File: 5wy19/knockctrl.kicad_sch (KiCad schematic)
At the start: 1 part, among them IC5 TP1C8101DW

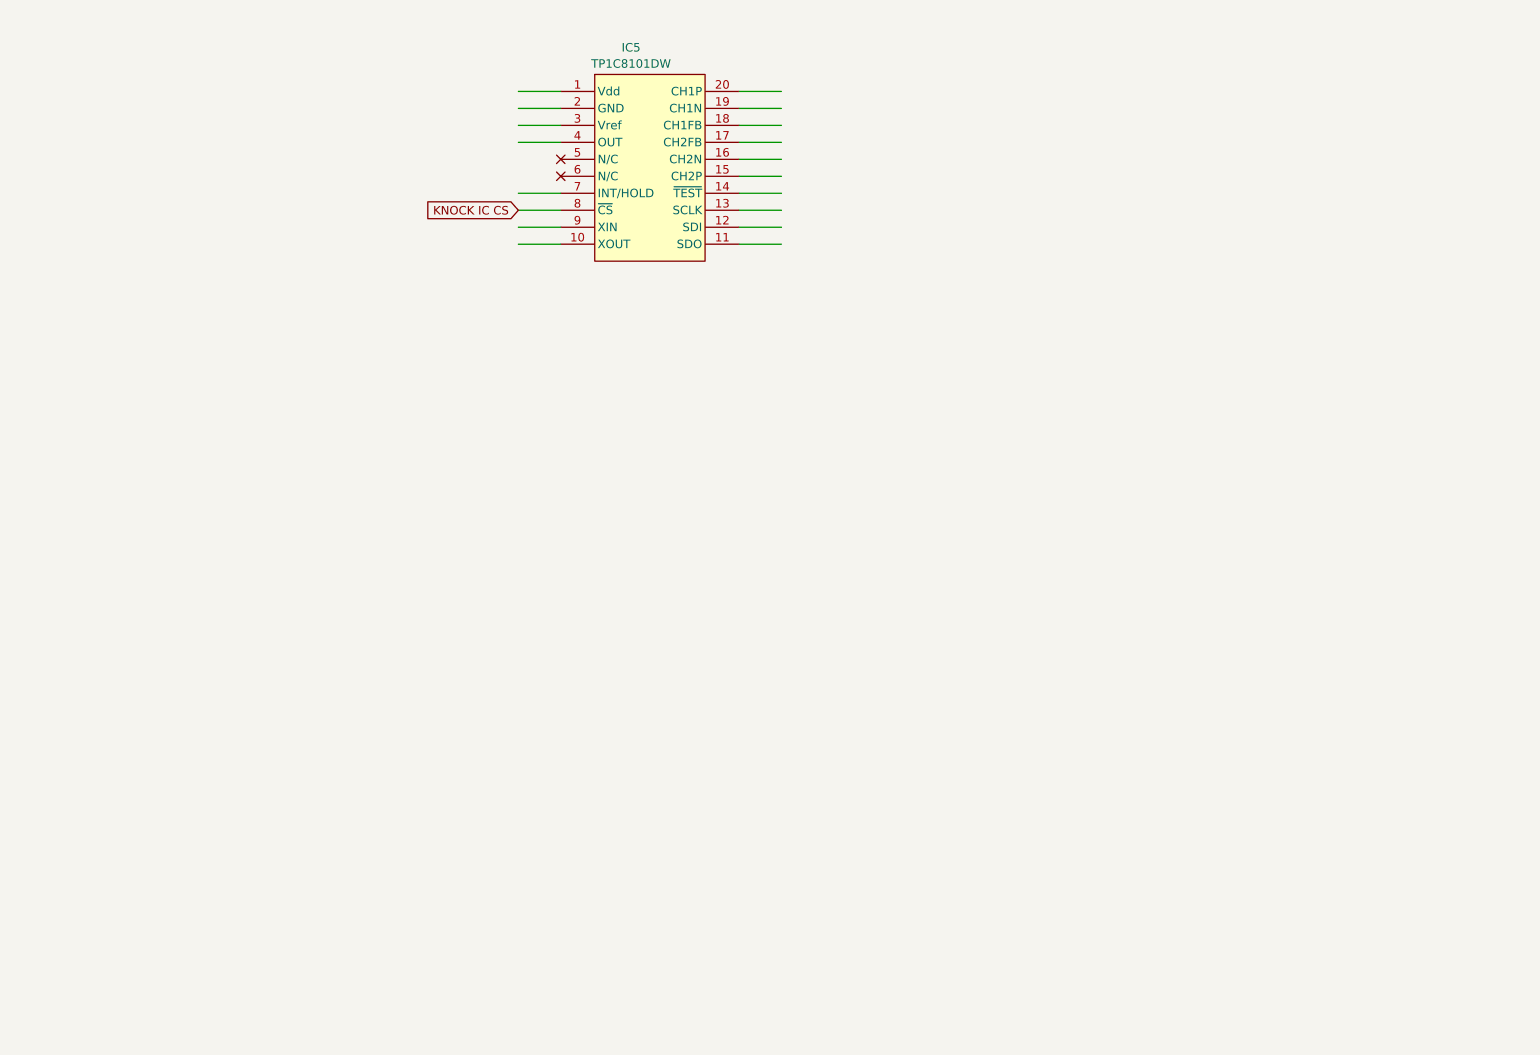
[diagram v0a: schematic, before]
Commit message: Further progress on MCU and connected circuits
Mostly sensors, knock control, some pins from the IO drivers and the unknown AMIS chip
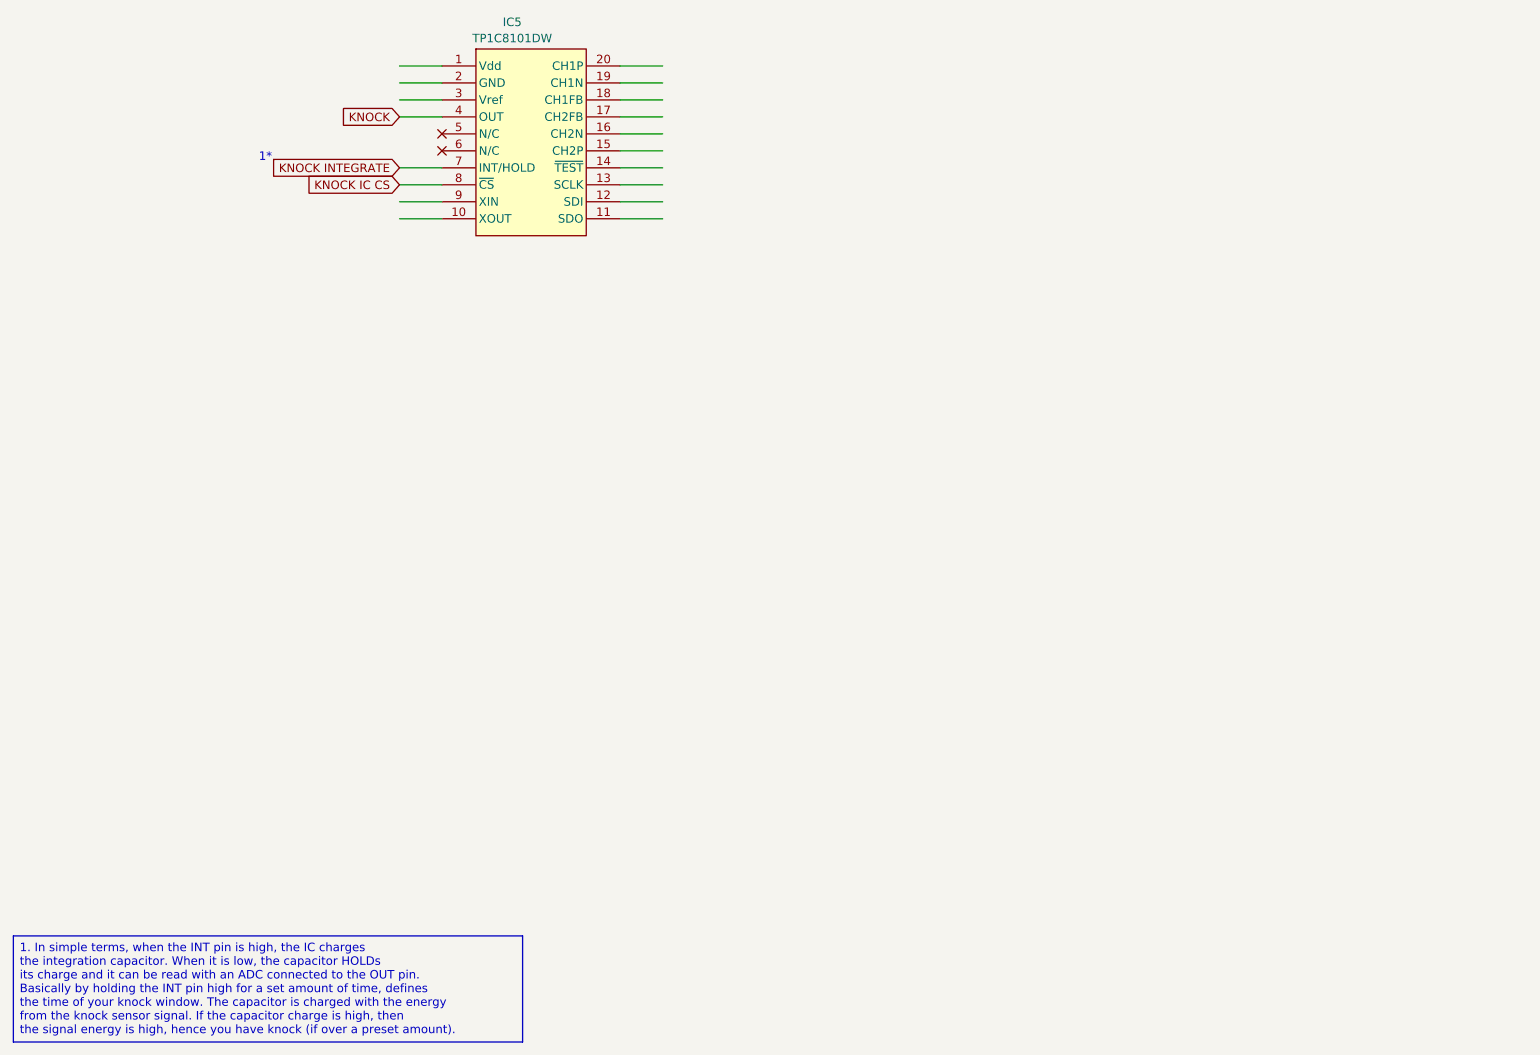
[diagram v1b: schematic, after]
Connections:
- net KNOCK: now reaches IC5.4 (OUT)
- net KNOCK INTEGRATE: now reaches IC5.7 (INT/HOLD)
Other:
- note added: "1*"
- moved on the sheet: IC5
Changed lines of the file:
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@@
 	(generator_version "9.0")
 	(paper "A4")
-	(wire
-		(pts
-			(xy 120.65 71.12) (xy 127 71.12)
-		)
-		(stroke
-			(width 0)
-			(type default)
-		)
-	)
-	(wire
-		(pts
-			(xy 120.65 66.04) (xy 127 66.04)
-		)
-		(stroke
-			(width 0)
-			(type default)
-		)
-	)
-	(wire
-		(pts
-			(xy 87.63 55.88) (xy 93.98 55.88)
-		)
-		(stroke
-			(width 0)
-			(type default)
-		)
-	)
-	(wire
-		(pts
-			(xy 120.65 58.42) (xy 127 58.42)
-		)
-		(stroke
-			(width 0)
-			(type default)
-		)
-	)
-	(wire
-		(pts
-			(xy 87.63 78.74) (xy 93.98 78.74)
-		)
-		(stroke
-			(width 0)
-			(type default)
-		)
-	)
-	(wire
-		(pts
-			(xy 87.63 71.12) (xy 93.98 71.12)
-		)
-		(stroke
-			(width 0)
-			(type default)
-		)
-	)
-	(wire
-		(pts
-			(xy 120.65 78.74) (xy 127 78.74)
-		)
-		(stroke
-			(width 0)
-			(type default)
-		)
-	)
-	(wire
-		(pts
-			(xy 120.65 55.88) (xy 127 55.88)
-		)
-		(stroke
-			(width 0)
-			(type default)
-		)
-	)
-	(wire
-		(pts
-			(xy 120.65 63.5) (xy 127 63.5)
-		)
-		(stroke
-			(width 0)
-			(type default)
-		)
-	)
-	(wire
-		(pts
-			(xy 87.63 60.96) (xy 93.98 60.96)
-		)
-		(stroke
-			(width 0)
-			(type default)
-		)
-	)
-	(wire
-		(pts
-			(xy 120.65 68.58) (xy 127 68.58)
-		)
-		(stroke
-			(width 0)
-			(type default)
-		)
-	)
-	(wire
-		(pts
-			(xy 120.65 73.66) (xy 127 73.66)
-		)
-		(stroke
-			(width 0)
-			(type default)
-		)
-	)
-	(wire
-		(pts
-			(xy 120.65 76.2) (xy 127 76.2)
-		)
-		(stroke
-			(width 0)
-			(type default)
-		)
-	)
-	(wire
-		(pts
-			(xy 120.65 60.96) (xy 127 60.96)
-		)
-		(stroke
-			(width 0)
-			(type default)
-		)
-	)
-	(wire
-		(pts
-			(xy 87.63 58.42) (xy 93.98 58.42)
-		)
-		(stroke
-			(width 0)
-			(type default)
-		)
-	)
-	(wire
-		(pts
-			(xy 87.63 76.2) (xy 93.98 76.2)
-		)
-		(stroke
-			(width 0)
-			(type default)
-		)
-	)
-	(wire
-		(pts
-			(xy 87.63 63.5) (xy 93.98 63.5)
-		)
-		(stroke
-			(width 0)
-			(type default)
-		)
-	)
-	(wire
-		(pts
-			(xy 87.63 73.66) (xy 93.98 73.66)
-		)
-		(stroke
-			(width 0)
-			(type default)
+	(text "1*"
+		(exclude_from_sim no)
+		(at 49.784 65.786 0)
+		(effects
+			(font
+				(size 1.27 1.27)
+			)
+		)
+	)
+	(text_box "1. In simple terms, when the INT pin is high, the IC charges\nthe integration capacitor. When it is low, the capacitor HOLDs\nits charge and it can be read with an ADC connected to the OUT pin.\nBasically by holding the INT pin high for a set amount of time, defines\nthe time of your knock window. The capacitor is charged with the energy\nfrom the knock sensor signal. If the capacitor charge is high, then \nthe signal energy is high, hence you have knock (if over a preset amount)."
+		(exclude_from_sim no)
+		(at 12.065 182.245 0)
+		(size 76.2 15.875)
+		(margins 0.9525 0.9525 0.9525 0.9525)
+		(stroke
+			(width 0)
+			(type solid)
+		)
+		(fill
+			(type none)
+		)
+		(effects
+			(font
+				(size 1.27 1.27)
+			)
+			(justify left top)
+		)
+	)
+	(wire
+		(pts
+			(xy 102.87 67.31) (xy 109.22 67.31)
+		)
+		(stroke
+			(width 0)
+			(type default)
+		)
+	)
+	(wire
+		(pts
+			(xy 102.87 62.23) (xy 109.22 62.23)
+		)
+		(stroke
+			(width 0)
+			(type default)
+		)
+	)
+	(wire
+		(pts
+			(xy 69.85 52.07) (xy 76.2 52.07)
+		)
+		(stroke
+			(width 0)
+			(type default)
+		)
+	)
+	(wire
+		(pts
+			(xy 102.87 54.61) (xy 109.22 54.61)
+		)
+		(stroke
+			(width 0)
+			(type default)
+		)
+	)
+	(wire
+		(pts
+			(xy 69.85 74.93) (xy 76.2 74.93)
+		)
+		(stroke
+			(width 0)
+			(type default)
+		)
+	)
+	(wire
+		(pts
+			(xy 69.85 67.31) (xy 76.2 67.31)
+		)
+		(stroke
+			(width 0)
+			(type default)
+		)
+	)
+	(wire
+		(pts
+			(xy 102.87 74.93) (xy 109.22 74.93)
+		)
+		(stroke
+			(width 0)
+			(type default)
+		)
+	)
+	(wire
+		(pts
+			(xy 102.87 52.07) (xy 109.22 52.07)
+		)
+		(stroke
+			(width 0)
+			(type default)
+		)
+	)
+	(wire
+		(pts
+			(xy 102.87 59.69) (xy 109.22 59.69)
+		)
+		(stroke
+			(width 0)
+			(type default)
+		)
+	)
+	(wire
+		(pts
+			(xy 69.85 57.15) (xy 76.2 57.15)
+		)
+		(stroke
+			(width 0)
+			(type default)
+		)
+	)
+	(wire
+		(pts
+			(xy 102.87 64.77) (xy 109.22 64.77)
+		)
+		(stroke
+			(width 0)
+			(type default)
+		)
+	)
+	(wire
+		(pts
+			(xy 102.87 69.85) (xy 109.22 69.85)
+		)
+		(stroke
+			(width 0)
+			(type default)
+		)
+	)
+	(wire
+		(pts
+			(xy 102.87 72.39) (xy 109.22 72.39)
+		)
+		(stroke
+			(width 0)
+			(type default)
+		)
+	)
+	(wire
+		(pts
+			(xy 102.87 57.15) (xy 109.22 57.15)
+		)
+		(stroke
+			(width 0)
+			(type default)
+		)
+	)
+	(wire
+		(pts
+			(xy 69.85 54.61) (xy 76.2 54.61)
+		)
+		(stroke
+			(width 0)
+			(type default)
+		)
+	)
+	(wire
+		(pts
+			(xy 69.85 72.39) (xy 76.2 72.39)
+		)
+		(stroke
+			(width 0)
+			(type default)
+		)
+	)
+	(wire
+		(pts
+			(xy 69.85 59.69) (xy 76.2 59.69)
+		)
+		(stroke
+			(width 0)
+			(type default)
+		)
+	)
+	(wire
+		(pts
+			(xy 69.85 69.85) (xy 76.2 69.85)
+		)
+		(stroke
+			(width 0)
+			(type default)
+		)
+	)
+	(global_label "KNOCK INTEGRATE"
+		(shape input)
+		(at 69.85 67.31 180)
+		(fields_autoplaced yes)
+		(effects
+			(font
+				(size 1.27 1.27)
+			)
+			(justify right)
+		)
+		(property "Intersheetrefs" "${INTERSHEET_REFS}"
+			(at 54.1043 67.31 0)
+			(effects
+				(font
+					(size 1.27 1.27)
+				)
+				(justify right)
+				(hide yes)
+			)
 		)
 	)
 	(global_label "KNOCK IC CS"
 		(shape input)
-		(at 87.63 73.66 180)
+		(at 69.85 69.85 180)
 		(fields_autoplaced yes)
 		(effects
@@
 		)
 		(property "Intersheetrefs" "${INTERSHEET_REFS}"
-			(at 71.8843 73.66 0)
+			(at 54.1043 69.85 0)
+			(effects
+				(font
+					(size 1.27 1.27)
+				)
+				(justify right)
+				(hide yes)
+			)
+		)
+	)
+	(global_label "KNOCK"
+		(shape input)
+		(at 69.85 59.69 180)
+		(fields_autoplaced yes)
+		(effects
+			(font
+				(size 1.27 1.27)
+			)
+			(justify right)
+		)
+		(property "Intersheetrefs" "${INTERSHEET_REFS}"
+			(at 54.1043 59.69 0)
 			(effects
 				(font
@@
 	(symbol
 		(lib_id "SIMK43:TP1C8101DW")
-		(at 107.95 67.31 0)
+		(at 90.17 63.5 0)
 		(unit 1)
 		(exclude_from_sim no)
@@
 		(fields_autoplaced yes)
 		(property "Reference" "IC5"
-			(at 104.4975 49.3225 0)
+			(at 86.7175 45.5125 0)
 			(effects
 				(font
@@
 		)
 		(property "Value" "TP1C8101DW"
-			(at 104.4975 51.7468 0)
+			(at 86.7175 47.9368 0)
 			(effects
 				(font
@@
 		)
 		(property "Footprint" ""
-			(at 107.95 67.31 0)
+			(at 90.17 63.5 0)
 			(effects
 				(font
@@
 		)
 		(property "Datasheet" ""
-			(at 107.95 67.31 0)
+			(at 90.17 63.5 0)
 			(effects
 				(font
@@
 		)
 		(property "Description" ""
-			(at 107.95 67.31 0)
-			(effects
-				(font
+			(at 90.17 63.5 0)
+			(effects
+				(font

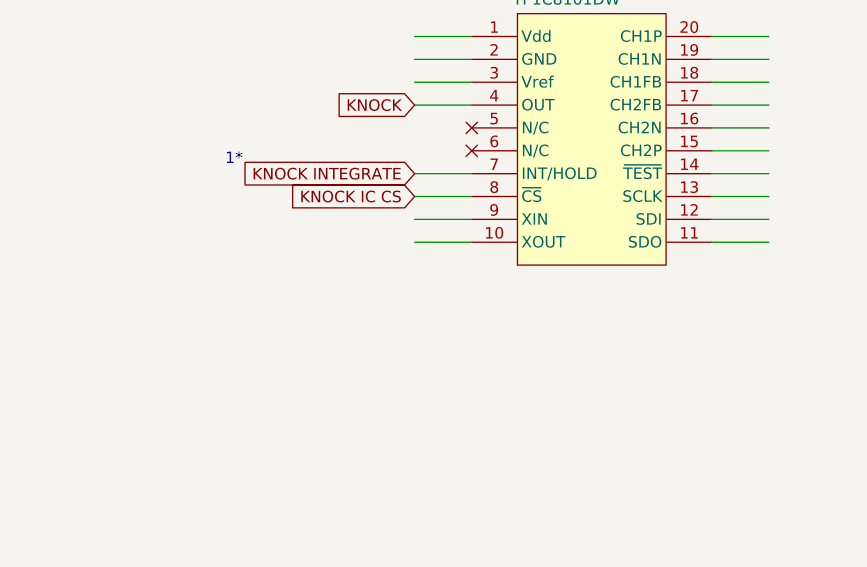
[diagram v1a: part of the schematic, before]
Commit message: Mapped out more pins of MCU and relevant circuits
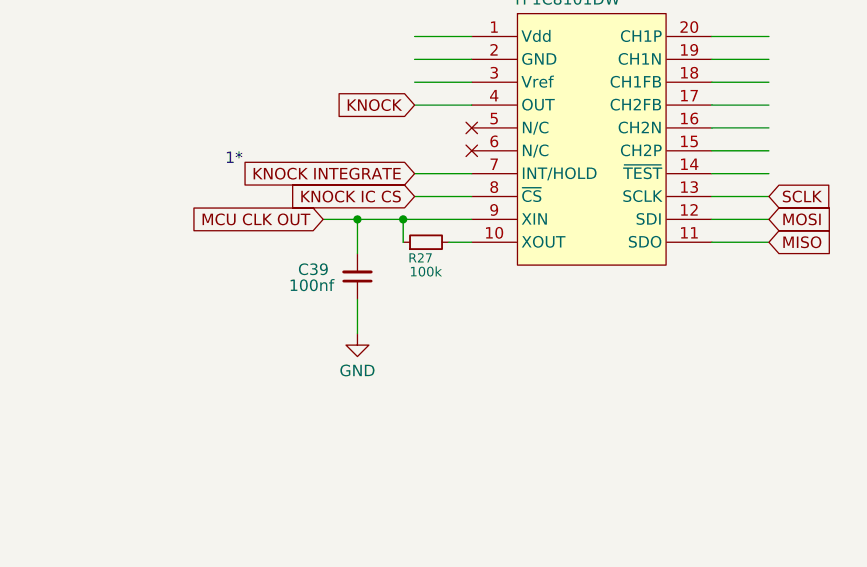
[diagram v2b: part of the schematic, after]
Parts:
- added C39: 100nf, symbol Device:C_Small
- added R27: 100k, symbol Device:R_Small
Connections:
- net at IC5.10 (XOUT): now also R27.2
- net MISO: now reaches IC5.11 (SDO)
- net MOSI: now reaches IC5.12 (SDI)
- net SCLK: now reaches IC5.13 (SCLK)
- net MCU CLK OUT: now reaches IC5.9 (XIN)
- net MCU CLK OUT: now also C39.2, R27.1
- new net GND: C39.1
